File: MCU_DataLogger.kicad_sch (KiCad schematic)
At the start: 0 parts

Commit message: passive component values
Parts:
- added BT1: Battery, symbol Device:Battery
- added C1, C4: 0.1uF, symbol Device:C
- added C2, C3: 22pF, symbol Device:C
- added C5: 100nF, symbol Device:C_Polarized
- added D1, D2: LED, symbol Device:LED
- added H1, H2, H3, H4: MountingHole, symbol Mechanical:MountingHole
- added R1, R2, R6: 10K, symbol Device:R
- added R3, R4: 4.7K, symbol Device:R
- added R5, R7: 330, symbol Device:R
- added U1: DS1337S+, SOIC127P600X175-8N, symbol DS1337S_:DS1337S+
- added U2, U3: 24LC1025, symbol Memory_EEPROM:24LC1025
- added U4: ATMEGA328P-AU, QFP80P900X900X120-32N, symbol ATMEGA328P-AU:ATMEGA328P-AU
- added Y1: 32.768 KHz, symbol Device:Crystal
- added Y2: 16 MHz, symbol Device:Crystal
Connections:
- new net: U4.21 (GND), U4.3 (GND), U4.5 (GND)
- new net: U4.4 (VCC), U4.6 (VCC)
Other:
- added sheet Connectors (connectors.kicad_sch)

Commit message: footprints
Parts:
- BT1: footprint (none) -> Connector_PinHeader_2.54mm:PinHeader_1x02_P2.54mm_Vertical
- C1, C2, C3, C4, C5: footprint (none) -> Capacitor_SMD:C_0805_2012Metric
- D1, D2: footprint (none) -> LED_SMD:LED_0805_2012Metric
- H1, H2, H3, H4: footprint (none) -> MountingHole:MountingHole_2.1mm
- R1, R2, R3, R4, R5, R6, R7: footprint (none) -> Resistor_SMD:R_0805_2012Metric
- U1: footprint SOIC127P600X175-8N -> FootPrints:SOIC127P600X175-8N
- U2, U3: footprint (none) -> Package_SO:SOIC-8_5.23x5.23mm_P1.27mm
- U4: footprint QFP80P900X900X120-32N -> FootPrints:QFP80P900X900X120-32N
- Y1, Y2: footprint (none) -> Crystal:Crystal_SMD_5032-2Pin_5.0x3.2mm_HandSoldering

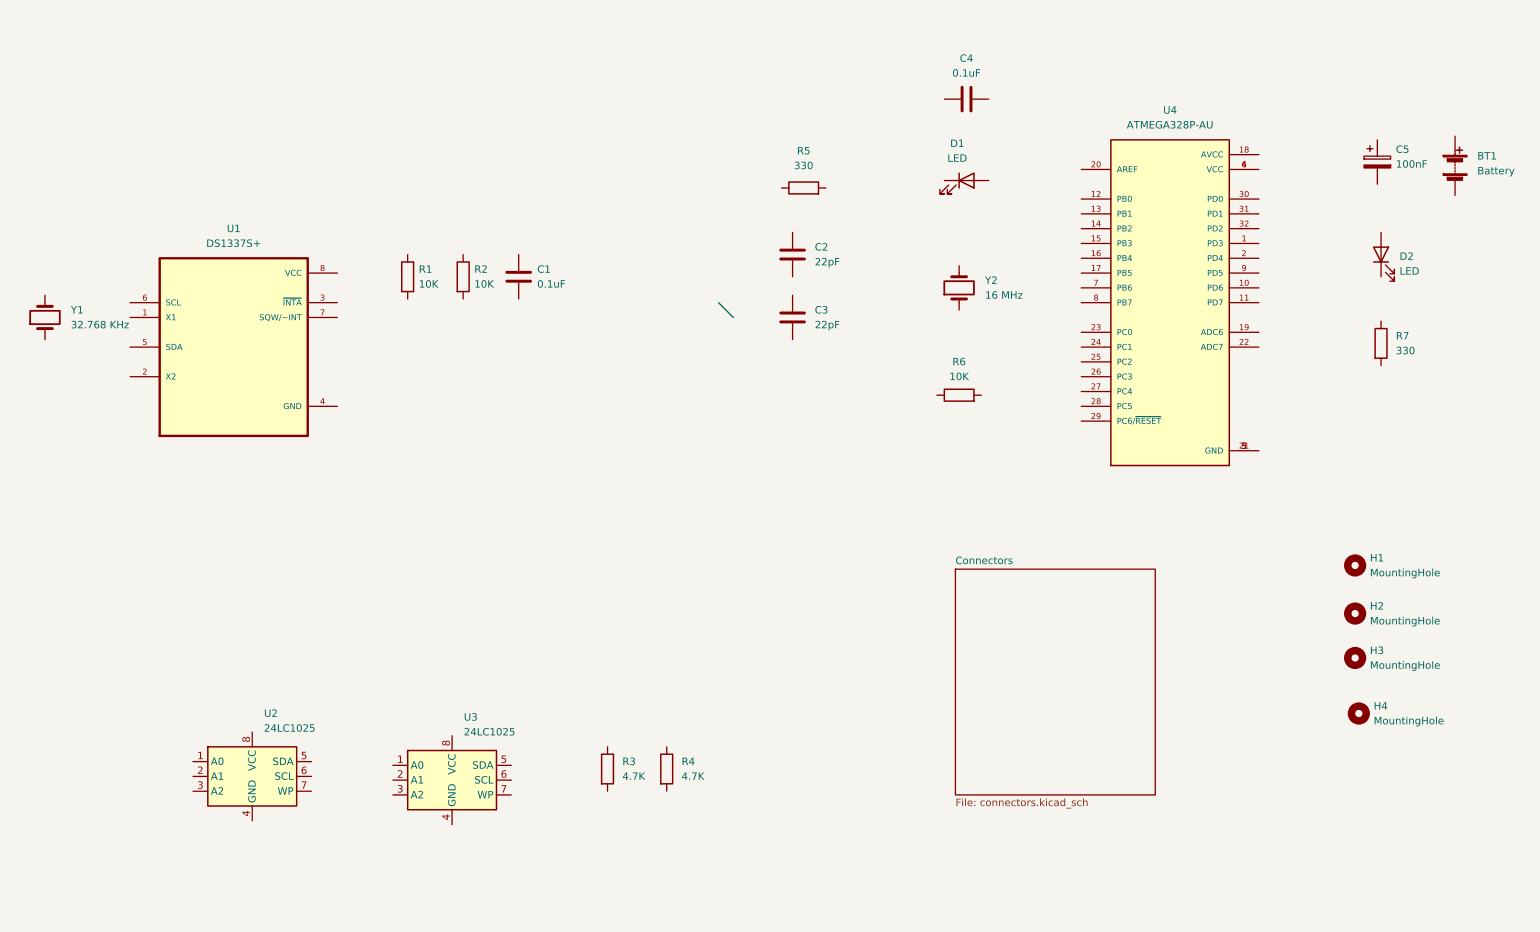
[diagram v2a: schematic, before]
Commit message: wiring of main sheet
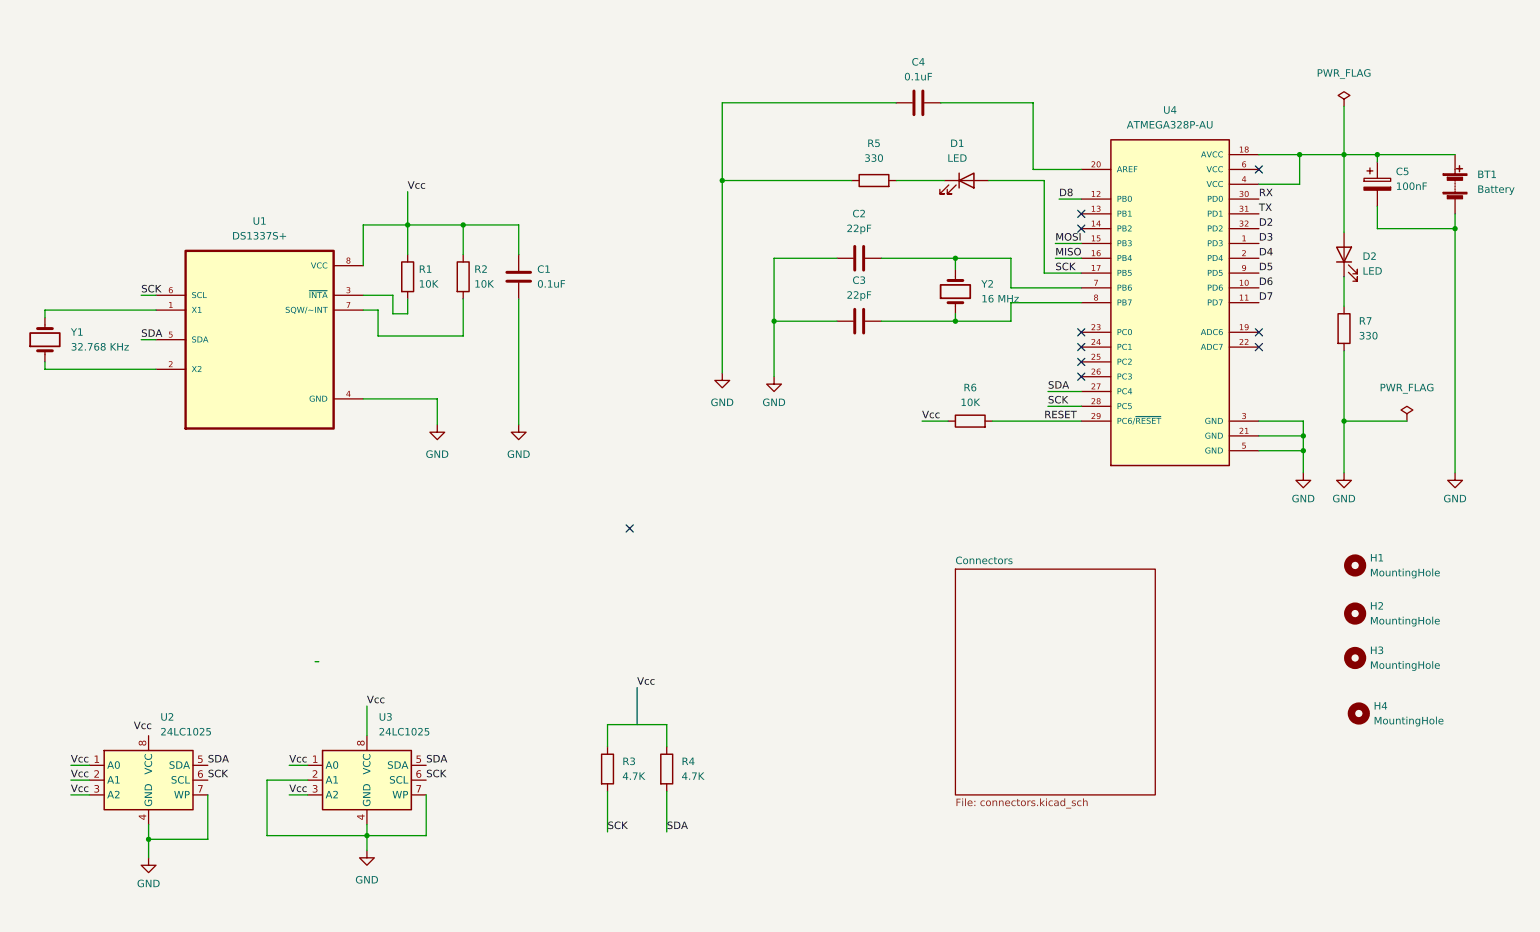
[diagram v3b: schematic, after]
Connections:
- net Vcc: now reaches U2.1 (A0)
- net Vcc: now also C1.1, R1.1, R2.1, R6.1, U1.8 (VCC), U2.2 (A1), U2.3 (A2), U3.1 (A0), U3.3 (A2), U3.8 (VCC)
- net GND: now reaches U2.4 (GND)
- net GND: now also BT1.2 (-), C1.2, C2.1, C3.1, C4.1, C5.2, R5.1, R7.2, U1.4 (GND), U2.7 (WP), U3.2 (A1), U3.4 (GND), U3.7 (WP), U4.21 (GND), U4.3 (GND), U4.5 (GND)
- net SDA: now reaches U2.5 (SDA)
- net SDA: now also R4.2, U1.5 (SDA), U3.5 (SDA), U4.27 (PC4)
- net SCK: now reaches U2.6 (SCL)
- net SCK: now also D1.2 (A), R3.2, U1.6 (SCL), U3.6 (SCL), U4.17 (PB5), U4.28 (PC5)
- net at D1.1 (K): now also R5.2
- net at C3.2: now also U4.8 (PB7), Y2.1
- net RESET: now reaches R6.2
- net RESET: now also U4.29 (PC6/~{RESET})
- net at C4.2: now also U4.20 (AREF)
- net at Y2.2: now also C2.2, U4.7 (PB6)
- net at R4.1: now also R3.1
- net at R7.1: now also D2.1 (K)
- net at BT1.1 (+): now also C5.1, D2.2 (A), U4.18 (AVCC), U4.4 (VCC)
- net at U1.1 (X1): now also Y1.2
- net at U1.2 (X2): now also Y1.1
- net at U1.3 (~{INTA}): now also R1.2
- net at U1.7 (SQW/~INT): now also R2.2
- net D3: now reaches U4.1 (PD3)
- net D6: now reaches U4.10 (PD6)
- net D7: now reaches U4.11 (PD7)
- net D8: now reaches U4.12 (PB0)
- net MOSI: now reaches U4.15 (PB3)
- net MISO: now reaches U4.16 (PB4)
- net D4: now reaches U4.2 (PD4)
- net RX: now reaches U4.30 (PD0)
- net TX: now reaches U4.31 (PD1)
- net D2: now reaches U4.32 (PD2)
- net at U4.6 (VCC): no longer U4.4 (VCC)
- net D5: now reaches U4.9 (PD5)
- no-connect marks 0 -> 10
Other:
- moved on the sheet: BT1, C2, C3, C4, C5, D2, R5, R6, R7, U1, U2, U3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

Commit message: finished wiring
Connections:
- net Vcc is gone; now on net VCC: C1.1, R1.1, R2.1, R6.1, U1.8 (VCC), U2.1 (A0), U2.2 (A1), U2.3 (A2), U3.1 (A0), U3.3 (A2), U3.8 (VCC)
- net VCC: now reaches U2.8 (VCC)
- net VCC: now also BT1.1 (+), C5.1, D2.2 (A), R3.1, R4.1, U4.18 (AVCC), U4.4 (VCC)
- no-connect marks 10 -> 9
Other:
- sheet Connectors ports: added D2, D3, D4, D5, D6, D7, D8, GND, MISO, MOSI, RESET, RX, SCK, SDA, TX, Vcc; removed none

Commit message: completed comments
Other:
- note added: "EEPROM"
- note added: "MCU"
- note added: "Mounting"
- note added: "Real time clock"
- moved on the sheet: H1, H2, H3, H4
